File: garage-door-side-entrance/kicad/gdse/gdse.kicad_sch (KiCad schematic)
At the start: 2 parts, among them J1 Screw_Terminal_01x10

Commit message: remove zips
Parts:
- added Z1: 5v Supply, symbol Mechanical:Housing
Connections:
- net GND: now reaches J1.1 (GND)
- net GND: now also A1.13 (GND), A1.18 (GND), A1.23 (GND), A1.28 (GND), A1.3 (GND), A1.38 (GND), A1.8 (GND)
- net at J1.2 (3v3): now also A1.36 (3V3)
- net +5V: now reaches A1.40 (VBUS)
- no-connect marks 0 -> 39
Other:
- title: Garage Door Side Entrance Controller  -> Garage Door Side Entrance Controller
- moved on the sheet: J1

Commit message: kicad work
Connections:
- net GND: now also J1.2 (Pin_2); no longer J1.1 (GND)
- net 3v3: now reaches A1.36 (3V3)
- net 3v3: now also J1.1 (Pin_1); no longer J1.2 (3v3)
- net Is Active LED | GP9 | 3-12: now reaches J1.3 (Pin_3)
- net Is Active LED | GP9 | 3-12: now also A1.12 (GPIO9)
- net OD Cover Button | GP10 |4-14: now reaches J1.4 (Pin_4)
- net OD Cover Button | GP10 |4-14: now also A1.14 (GPIO10)
- net Run LED | GP11 | 5-15: now reaches J1.5 (Pin_5)
- net Run LED | GP11 | 5-15: now also A1.15 (GPIO11)
- net ID Cover Button | GP12 | 6-16: now reaches J1.6 (Pin_6)
- net ID Cover Button | GP12 | 6-16: now also A1.16 (GPIO12)
- net Locked LED | GP13 | 7-17: now reaches J1.7 (Pin_7)
- net Locked LED | GP13 | 7-17: now also A1.17 (GPIO13)
- net Locked Button | GP14 | 8-19: now reaches J1.8 (Pin_8)
- net Locked Button | GP14 | 8-19: now also A1.19 (GPIO14)
- no-connect marks 39 -> 27
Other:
- moved on the sheet: A1, Z1

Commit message: cleanup
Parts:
- added BL1: ~, symbol gdse_library:Button_w/LED
- added BR1: ~, symbol gdse_library:Button_w/RGB
- added CN1: ~, symbol gdse_library:Block_Connector
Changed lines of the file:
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@@
+	)
+	(symbol
+		(lib_id "gdse_library:Button_w/RGB")
+		(at 58.42 82.55 0)
+		(unit 1)
+		(exclude_from_sim no)
+		(in_bom yes)
+		(on_board yes)
+		(dnp no)
+		(fields_autoplaced yes)
+		(property "Reference" "BR1"
+			(at 55.88 72.39 0)
+			(effects
+				(font
+					(size 1.27 1.27)
+				)
+			)
+		)
+		(property "Value" "~"
+			(at 55.88 74.93 0)
+			(effects
+				(font
+					(size 1.27 1.27)
+				)
+			)
+		)
+		(property "Footprint" ""
+			(at 58.42 82.55 0)
+			(effects
+				(font
+					(size 1.27 1.27)
+				)
+				(hide yes)
+			)
+		)
+		(property "Datasheet" ""
+			(at 58.42 82.55 0)
+			(effects
+				(font
+					(size 1.27 1.27)
+				)
+				(hide yes)
+			)
+		)
+		(property "Description" ""
+			(at 58.42 82.55 0)
+			(effects
+				(font
+					(size 1.27 1.27)
+				)
+				(hide yes)
+			)
+		)
+		(pin "4"
+		)
+		(pin "2"
+		)
+		(pin "5"
+		)
+		(pin "6"
+		)
+		(pin "1"
+		)
+		(pin "3"
+		)
+		(instances
+			(project ""
+				(path "/d82d5400-656c-4ace-93b6-f85bceb9c5dc"
+					(reference "BR1")
+					(unit 1)
+				)
+			)
+		)
+	)
+	(symbol
+		(lib_id "gdse_library:Button_w/LED")
+		(at 62.23 59.69 0)
+		(unit 1)
+		(exclude_from_sim no)
+		(in_bom yes)
+		(on_board yes)
+		(dnp no)
+		(fields_autoplaced yes)
+		(property "Reference" "BL1"
+			(at 59.69 50.8 0)
+			(effects
+				(font
+					(size 1.27 1.27)
+				)
+			)
+		)
+		(property "Value" "~"
+			(at 59.69 53.34 0)
+			(effects
+				(font
+					(size 1.27 1.27)
+				)
+			)
+		)
+		(property "Footprint" ""
+			(at 62.23 59.69 0)
+			(effects
+				(font
+					(size 1.27 1.27)
+				)
+				(hide yes)
+			)
+		)
+		(property "Datasheet" ""
+			(at 62.23 59.69 0)
+			(effects
+				(font
+					(size 1.27 1.27)
+				)
+				(hide yes)
+			)
+		)
+		(property "Description" ""
+			(at 62.23 59.69 0)
+			(effects
+				(font
+					(size 1.27 1.27)
+				)
+				(hide yes)
+			)
+		)
+		(pin "5"
+		)
+		(pin "3"
+		)
+		(pin "1"
+		)
+		(pin "4"
+		)
+		(pin "2"
+		)
+		(instances
+			(project ""
+				(path "/d82d5400-656c-4ace-93b6-f85bceb9c5dc"
+					(reference "BL1")
+					(unit 1)
+				)
+			)
+		)
 	)
 	(symbol
@@
 					(unit 1)
 				)
+			)
+		)
+	)
+	(symbol
+		(lib_id "gdse_library:Block_Connector")
+		(at 63.5 41.91 0)
+		(unit 1)
+		(exclude_from_sim no)
+		(in_bom yes)
+		(on_board yes)
+		(dnp no)
+		(fields_autoplaced yes)
+		(property "Reference" "CN1"
+			(at 63.5 34.29 0)
+			(effects
+				(font
+					(size 1.27 1.27)
+				)
+			)
+		)
+		(property "Value" "~"
+			(at 63.5 36.83 0)
+			(effects
+				(font
+					(size 1.27 1.27)
+				)
+			)
+		)
+		(property "Footprint" ""
+			(at 63.5 41.91 0)
+			(effects
+				(font
+					(size 1.27 1.27)
+				)
+				(hide yes)
+			)
+		)
+		(property "Datasheet" ""
+			(at 63.5 41.91 0)
+			(effects
+				(font
+					(size 1.27 1.27)
+				)
+				(hide yes)
+			)
+		)
+		(property "Description" ""
+			(at 63.5 41.91 0)
+			(effects
+				(font
+					(size 1.27 1.27)
+				)
+				(hide yes)
+			)
+		)
+		(pin "6"
+		)
+		(pin "5"
+		)
+		(pin "4"
+		)
+		(pin "2"
+		)
+		(pin "1"
+		)
+		(pin "3"
+		)
+		(instances
+			(project ""
+				(path "/d82d5400-656c-4ace-93b6-f85bceb9c5dc"
+					(reference "CN1")
+					(unit 1)
+				)

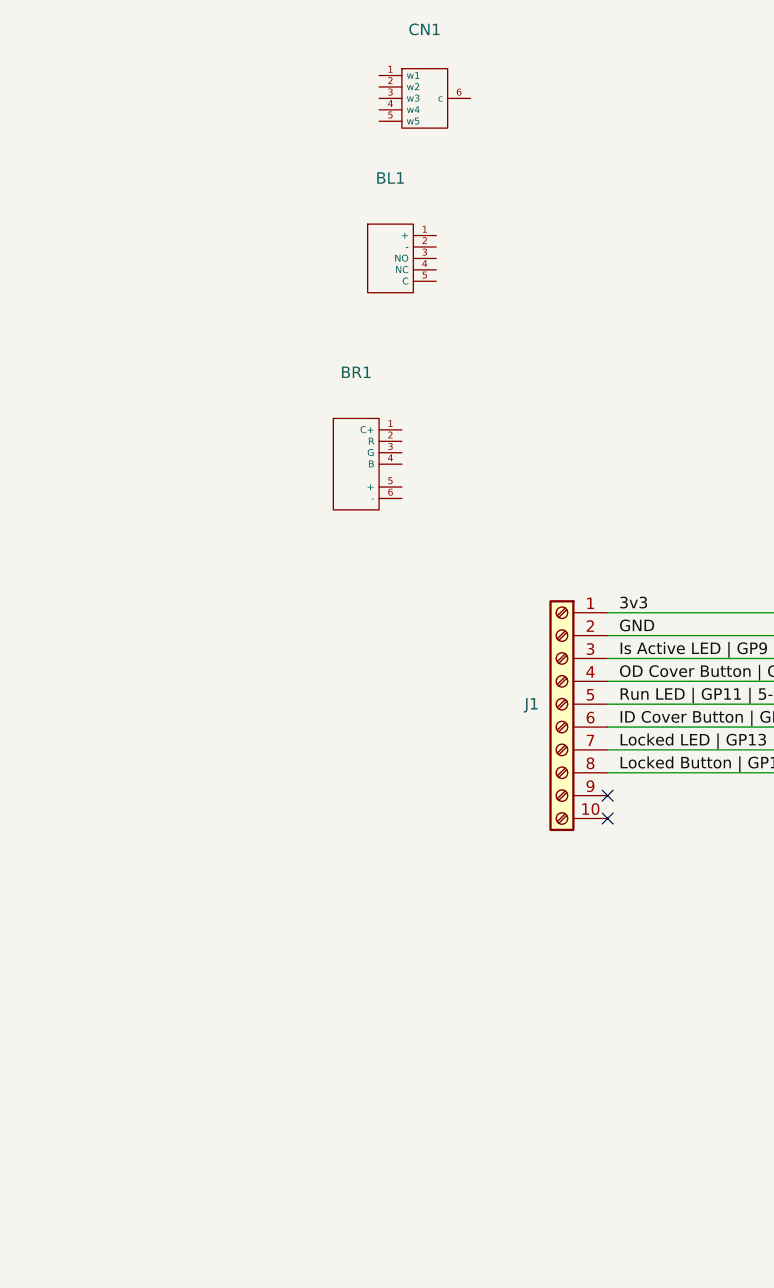
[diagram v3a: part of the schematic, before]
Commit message: added buttons to sch
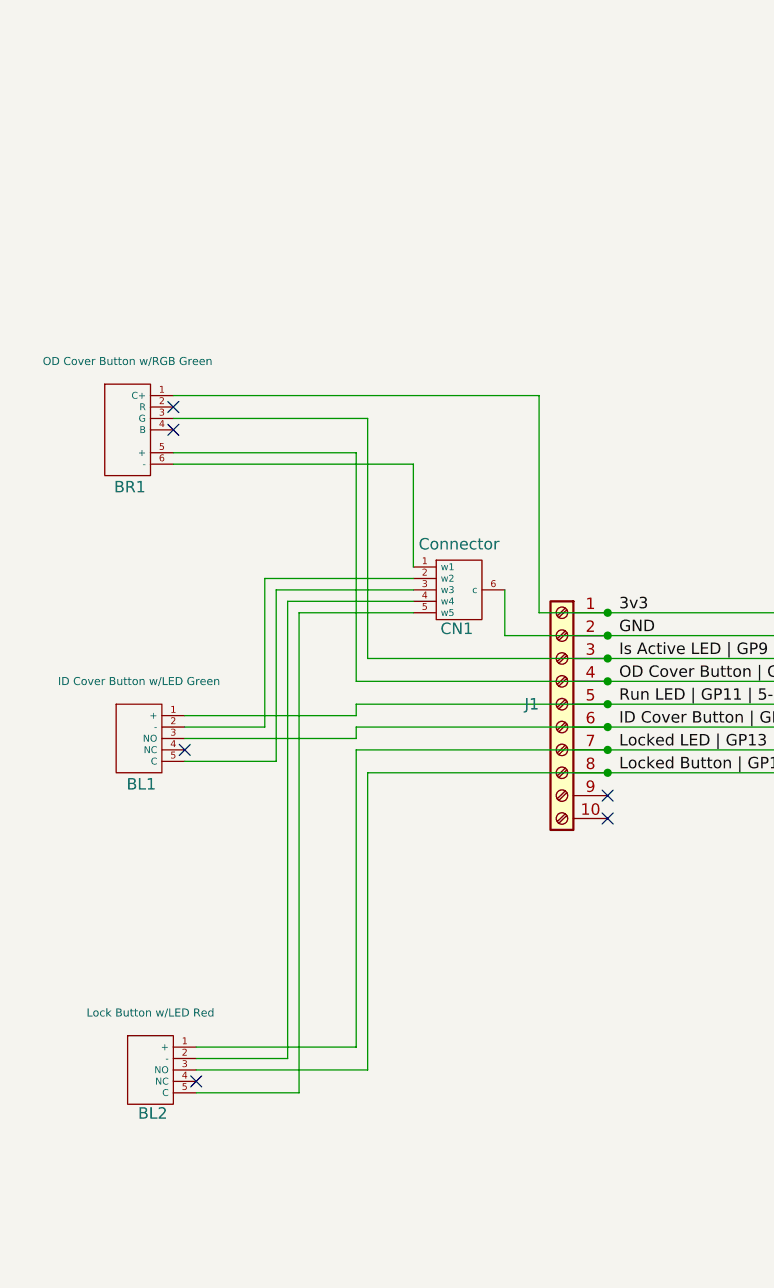
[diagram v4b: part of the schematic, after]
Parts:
- added BL2: Lock Button w/LED Red, symbol gdse_library:Button_w/LED
- BL1: value ~ -> ID Cover Button w/LED Green
- BR1: value ~ -> OD Cover Button w/RGB Green
- CN1: value ~ -> Connector
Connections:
- net 3v3: now also BR1.1 (C+)
- net GND: now also CN1.6 (c)
- net ID Cover Button | GP12 | 6-16: now also BL1.3 (NO)
- net Is Active LED | GP9 | 3-12: now also BR1.3 (G)
- net Locked Button | GP14 | 8-19: now also BL2.3 (NO)
- net Locked LED | GP13 | 7-17: now also BL2.1 (+)
- net OD Cover Button | GP10 |4-14: now also BR1.5 (+)
- net Run LED | GP11 | 5-15: now also BL1.1 (+)
- net at BR1.6 (-): now also CN1.1 (w1)
- net at BL1.2 (-): now also CN1.2 (w2)
- net at BL1.5 (C): now also CN1.3 (w3)
- net at CN1.4 (w4): now also BL2.2 (-)
- net at CN1.5 (w5): now also BL2.5 (C)
- no-connect marks 27 -> 31
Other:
- moved on the sheet: BL1, BR1, CN1

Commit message: kcad work
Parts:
- A1: footprint Module:RaspberryPi_Pico_W_SMD_HandSolder -> Module:RaspberryPi_Pico_Common_THT
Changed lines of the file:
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@@
 		(exclude_from_sim no)
 		(in_bom yes)
-		(on_board yes)
+		(on_board no)
 		(dnp no)
 		(property "Reference" "CN1"
@@
 			)
 		)
-		(property "Footprint" "Module:RaspberryPi_Pico_W_SMD_HandSolder"
+		(property "Footprint" "Module:RaspberryPi_Pico_Common_THT"
 			(at 163.83 162.56 0)
 			(effects

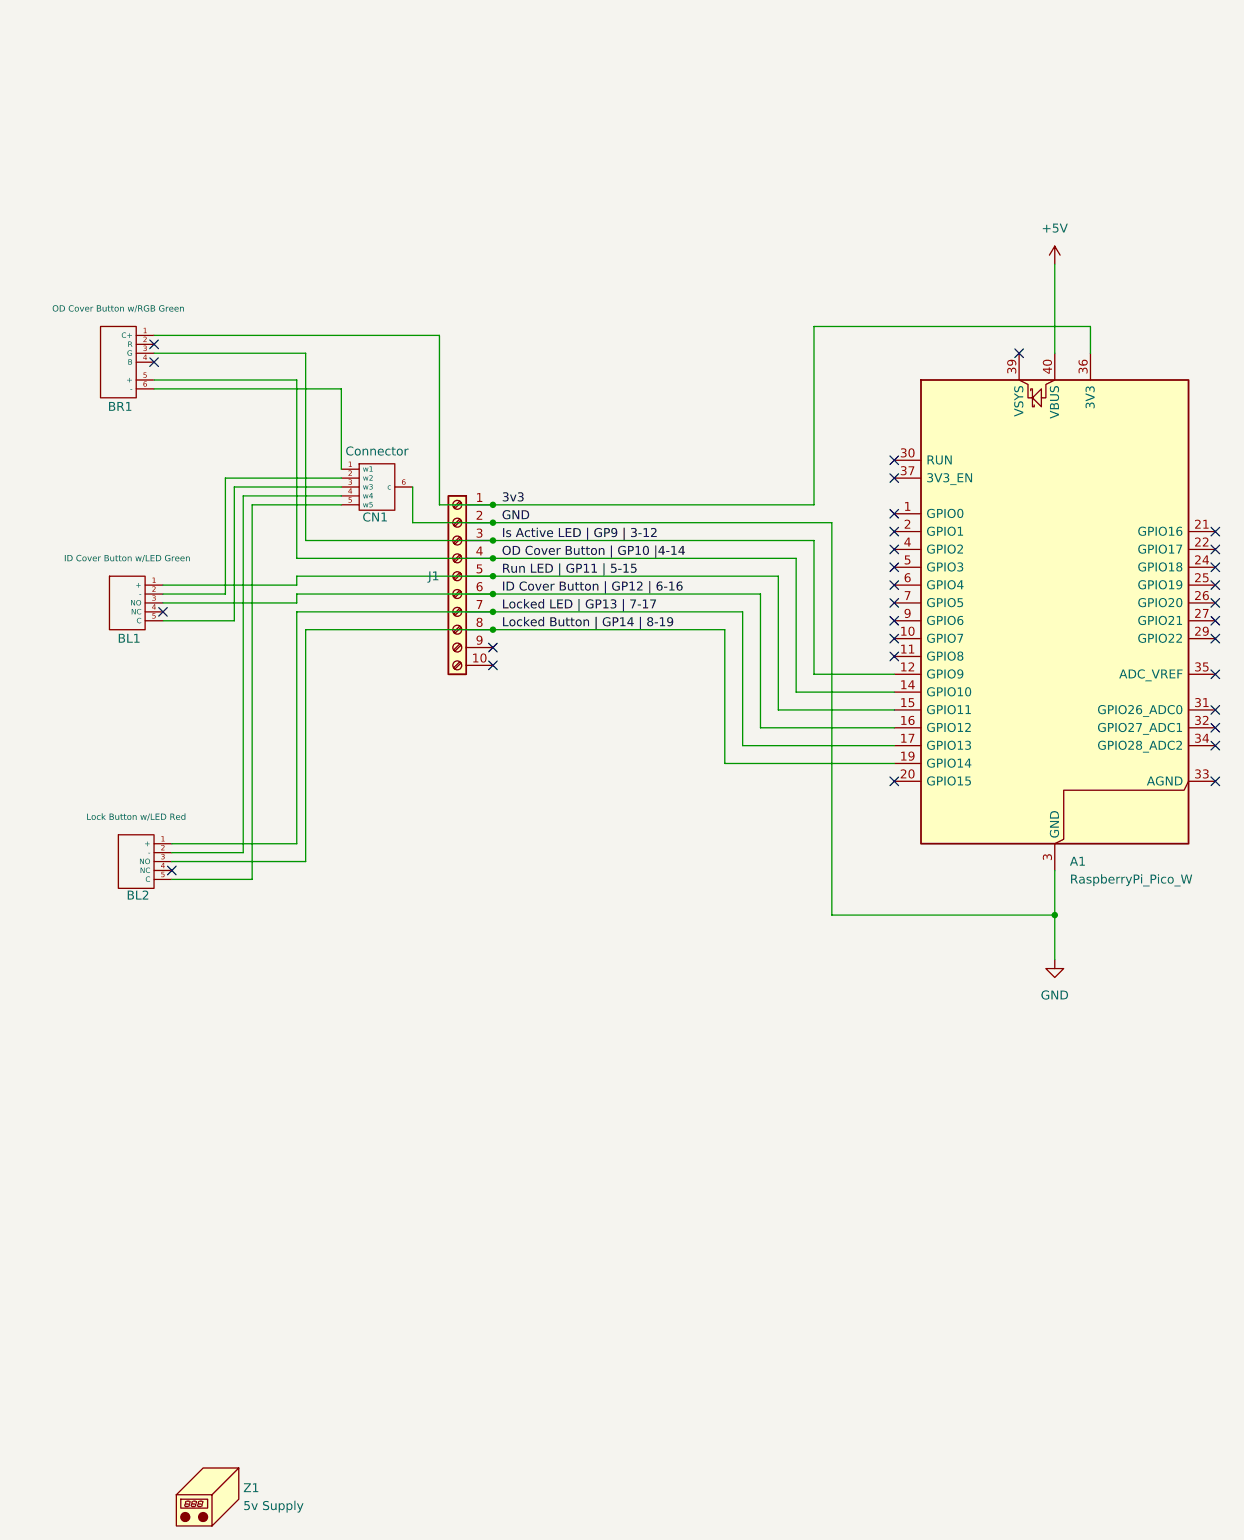
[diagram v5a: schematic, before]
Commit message: add jst xh connectors
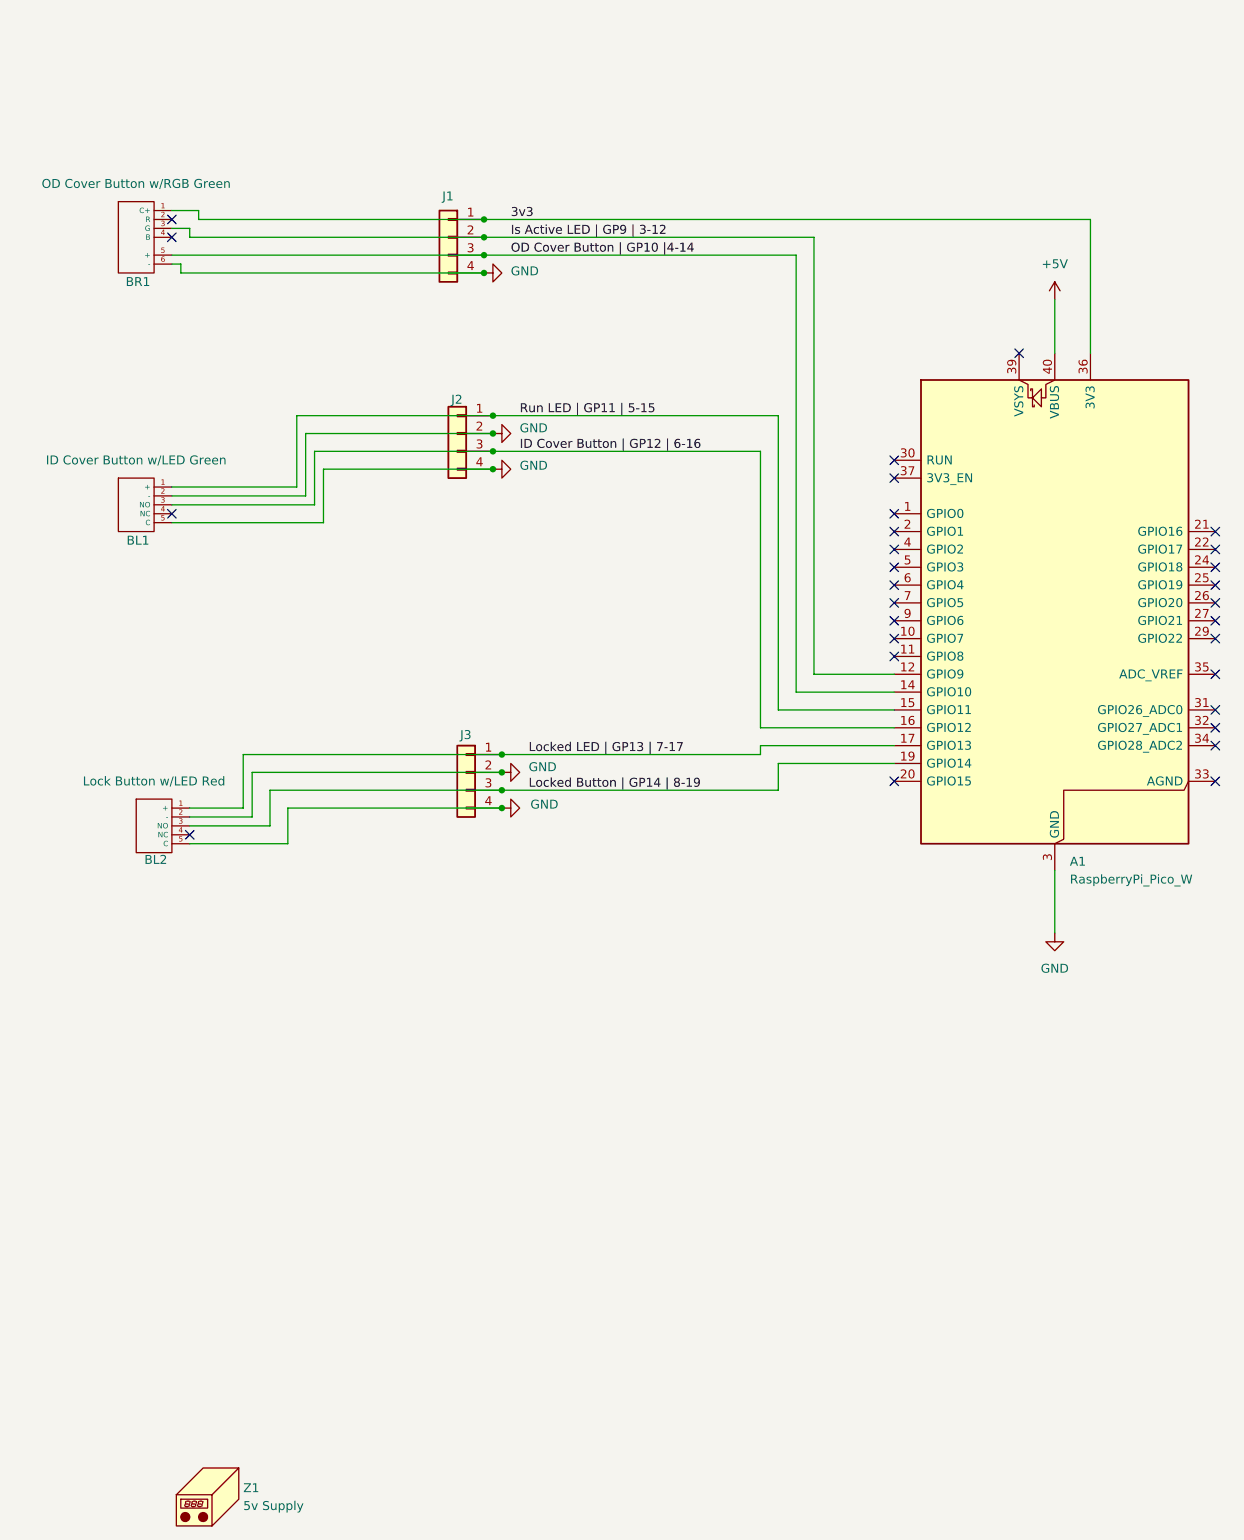
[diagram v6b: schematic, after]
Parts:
- removed CN1: Connector, symbol gdse_library:Block_Connector
- removed J1: Screw_Terminal_01x10, TerminalBlock:TerminalBlock_Xinya_XY308-2.54-10P_1x10_P2.54mm_Horizontal, symbol Connector:Screw_Terminal_01x10
- added J1, J2, J3: Conn_01x04, Connector_JST:JST_XH_B4B-XH-A_1x04_P2.50mm_Vertical, symbol Connector_Generic:Conn_01x04
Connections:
- net 3v3: now also J1.1 (Pin_1)
- net GND: now also BL1.2 (-), BL1.5 (C), BL2.2 (-), BL2.5 (C), BR1.6 (-), J1.4 (Pin_4), J2.2 (Pin_2), J2.4 (Pin_4), J3.2 (Pin_2), J3.4 (Pin_4)
- net ID Cover Button | GP12 | 6-16: now also J2.3 (Pin_3)
- net Is Active LED | GP9 | 3-12: now also J1.2 (Pin_2)
- net Locked Button | GP14 | 8-19: now also J3.3 (Pin_3)
- net Locked LED | GP13 | 7-17: now also J3.1 (Pin_1)
- net OD Cover Button | GP10 |4-14: now also J1.3 (Pin_3)
- net Run LED | GP11 | 5-15: now also J2.1 (Pin_1)
- no-connect marks 31 -> 29
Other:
- moved on the sheet: BL1, BL2, BR1

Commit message: gdo side entrance proto1
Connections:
- net ID Cover Button | GP12 | 6-16 renamed ID Cover Button | GP12 | P16
- net Is Active LED | GP9 | 3-12 renamed Is Active LED | GP9 | P12
- net Locked Button | GP14 | 8-19 renamed Locked Button | GP14 | P19
- net Locked LED | GP13 | 7-17 renamed Locked LED | GP13 | P17
- net OD Cover Button | GP10 |4-14 renamed OD Cover Button | GP10 | P14
- net Run LED | GP11 | 5-15 renamed Run LED | GP11 | P15
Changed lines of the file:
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@@
 		)
 	)
-	(label "Is Active LED | GP9 | 3-12"
+	(label "Is Active LED | GP9 | P12"
 		(at 86.36 60.96 0)
 		(effects
@@
 		)
 	)
-	(label "Run LED | GP11 | 5-15"
+	(label "Run LED | GP11 | P15"
 		(at 87.63 86.36 0)
 		(effects
@@
 		)
 	)
-	(label "ID Cover Button | GP12 | 6-16"
+	(label "ID Cover Button | GP12 | P16"
 		(at 87.63 91.44 0)
 		(effects
@@
 		)
 	)
-	(label "OD Cover Button | GP10 |4-14"
+	(label "OD Cover Button | GP10 | P14"
 		(at 86.36 63.5 0)
 		(effects
@@
 		)
 	)
-	(label "Locked Button | GP14 | 8-19"
+	(label "Locked Button | GP14 | P19"
 		(at 88.9 139.7 0)
 		(effects
@@
 		)
 	)
-	(label "Locked LED | GP13 | 7-17"
+	(label "Locked LED | GP13 | P17"
 		(at 88.9 134.62 0)
 		(effects
